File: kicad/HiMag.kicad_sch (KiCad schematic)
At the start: 2 parts, among them U1801 TLE493D-W2B6

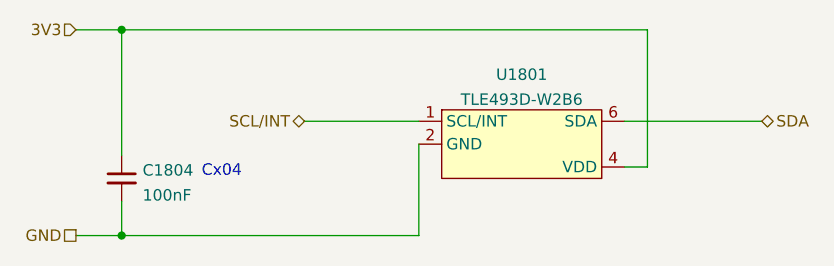
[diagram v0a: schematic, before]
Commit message: Broke down sensor block into a tree of sheets
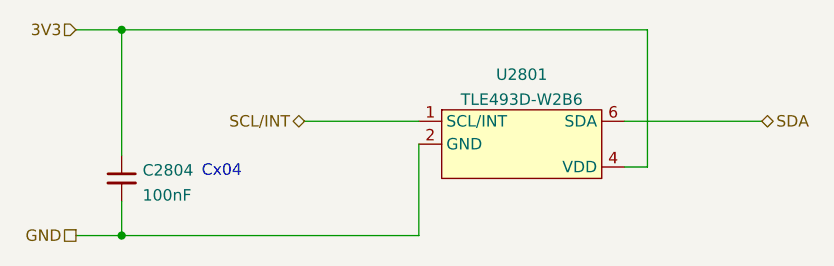
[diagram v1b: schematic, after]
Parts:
- renumbered C1804 to C2804, U1801 to U2801
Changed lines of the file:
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@@
   (symbol (lib_id "Device:C_Small") (at 93.98 107.95 0)
     (in_bom yes) (on_board yes) (fields_autoplaced)
-    (property "Reference" "C1804" (id 0) (at 96.3041 107.0478 0)
+    (property "Reference" "C2804" (id 0) (at 96.3041 107.0478 0)
       (effects (font (size 1.27 1.27)) (justify left))
     )
@@
   (symbol (lib_id "KwanSystems:TLE493D-W2B6") (at 138.43 104.14 0)
     (in_bom yes) (on_board yes) (fields_autoplaced)
-    (property "Reference" "U1801" (id 0) (at 138.43 96.4143 0))
+    (property "Reference" "U2801" (id 0) (at 138.43 96.4143 0))
     (property "Value" "TLE493D-W2B6" (id 1) (at 138.43 99.1894 0))
     (property "Footprint" "Package_TO_SOT_SMD:SOT-23-6" (id 2) (at 138.43 114.3 0)

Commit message: Added Digikey references
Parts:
- C2804: Digikey (none) -> 399-C0402C104K4RAC7411CT-ND
- U2801: Digikey (none) -> TLE493DW2B6A3HTSA1CT-ND; Purpose (none) -> High-field magnetic sensor
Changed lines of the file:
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@@
+      (effects (font (size 1.27 1.27)) hide)
+    )
+    (property "Digikey" "399-C0402C104K4RAC7411CT-ND" (id 4) (at 93.98 107.95 0)
       (effects (font (size 1.27 1.27)) hide)
     )
@@
       (effects (font (size 1.27 1.27)) hide)
     )
+    (property "Digikey" "TLE493DW2B6A3HTSA1CT-ND" (id 4) (at 138.43 104.14 0)
+      (effects (font (size 1.27 1.27)) hide)
+    )
+    (property "Purpose" "High-field magnetic sensor" (id 5) (at 138.43 104.14 0)
+      (effects (font (size 1.27 1.27)) hide)
+    )

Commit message: Added a purpose field to bypass capacitors
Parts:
- C2804: Purpose (none) -> HiMag bypass
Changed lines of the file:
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@@
+      (effects (font (size 1.27 1.27)) hide)
+    )
+    (property "Purpose" "HiMag bypass" (id 5) (at 93.98 107.95 0)
       (effects (font (size 1.27 1.27)) hide)
     )

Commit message: Checkin before branch
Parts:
- renumbered C2804 to C704, U2801 to U701
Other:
- company: (none) -> Kwan Systems
- title: (none) -> Rollercoasterometer
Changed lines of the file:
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@@
 (kicad_sch (version 20211123) (generator eeschema)
-  (paper "A4")
+  (paper "USLetter")
+  (title_block
+    (title "Rollercoasterometer")
+    (date "2022-10-07")
+    (company "Kwan Systems")
+  )
   (junction (at 93.98 91.44) (diameter 0) (color 0 0 0 0)
   )
@@
     (effects (font (size 1.27 1.27)) (justify right))
   )
-  (symbol (lib_id "Device:C_Small") (at 93.98 107.95 0)
+  (symbol (lib_id "Device:C_Small") (at 93.98 107.95 0) (unit 1)
     (in_bom yes) (on_board yes) (fields_autoplaced)
-    (property "Reference" "C2804" (id 0) (at 96.3041 107.0478 0)
+    (property "Reference" "C704" (id 0) (at 96.3041 107.1216 0)
       (effects (font (size 1.27 1.27)) (justify left))
     )
-    (property "Value" "100nF" (id 1) (at 96.3041 109.8229 0)
+    (property "Value" "100nF" (id 1) (at 96.3041 109.6585 0)
       (effects (font (size 1.27 1.27)) (justify left))
     )
@@
     (pin "2")
   )
-  (symbol (lib_id "KwanSystems:TLE493D-W2B6") (at 138.43 104.14 0)
+  (symbol (lib_id "KwanSystems:TLE493D-W2B6") (at 138.43 104.14 0) (unit 1)
     (in_bom yes) (on_board yes) (fields_autoplaced)
-    (property "Reference" "U2801" (id 0) (at 138.43 96.4143 0))
-    (property "Value" "TLE493D-W2B6" (id 1) (at 138.43 99.1894 0))
+    (property "Reference" "U701" (id 0) (at 138.43 96.681 0))
+    (property "Value" "TLE493D-W2B6" (id 1) (at 138.43 99.2179 0))
     (property "Footprint" "Package_TO_SOT_SMD:SOT-23-6" (id 2) (at 138.43 114.3 0)
       (effects (font (size 1.27 1.27)) hide)
